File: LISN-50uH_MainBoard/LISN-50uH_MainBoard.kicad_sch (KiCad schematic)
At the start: 85 parts, among them J1 Faston Tab 4.8mm, J10 Conn_Coaxial, J11 Conn_01x03_Pin, J2 Faston Tab 4.8mm, J3 Faston Tab 4.8mm, J4 Faston Tab 4.8mm, J5 Conn_Coaxial, J6 Conn_Coaxial, J7 Faston Tab 4.8mm, J8 Faston Tab 4.8mm, J9 Conn_Coaxial, SW1 SW_DPDT_x2

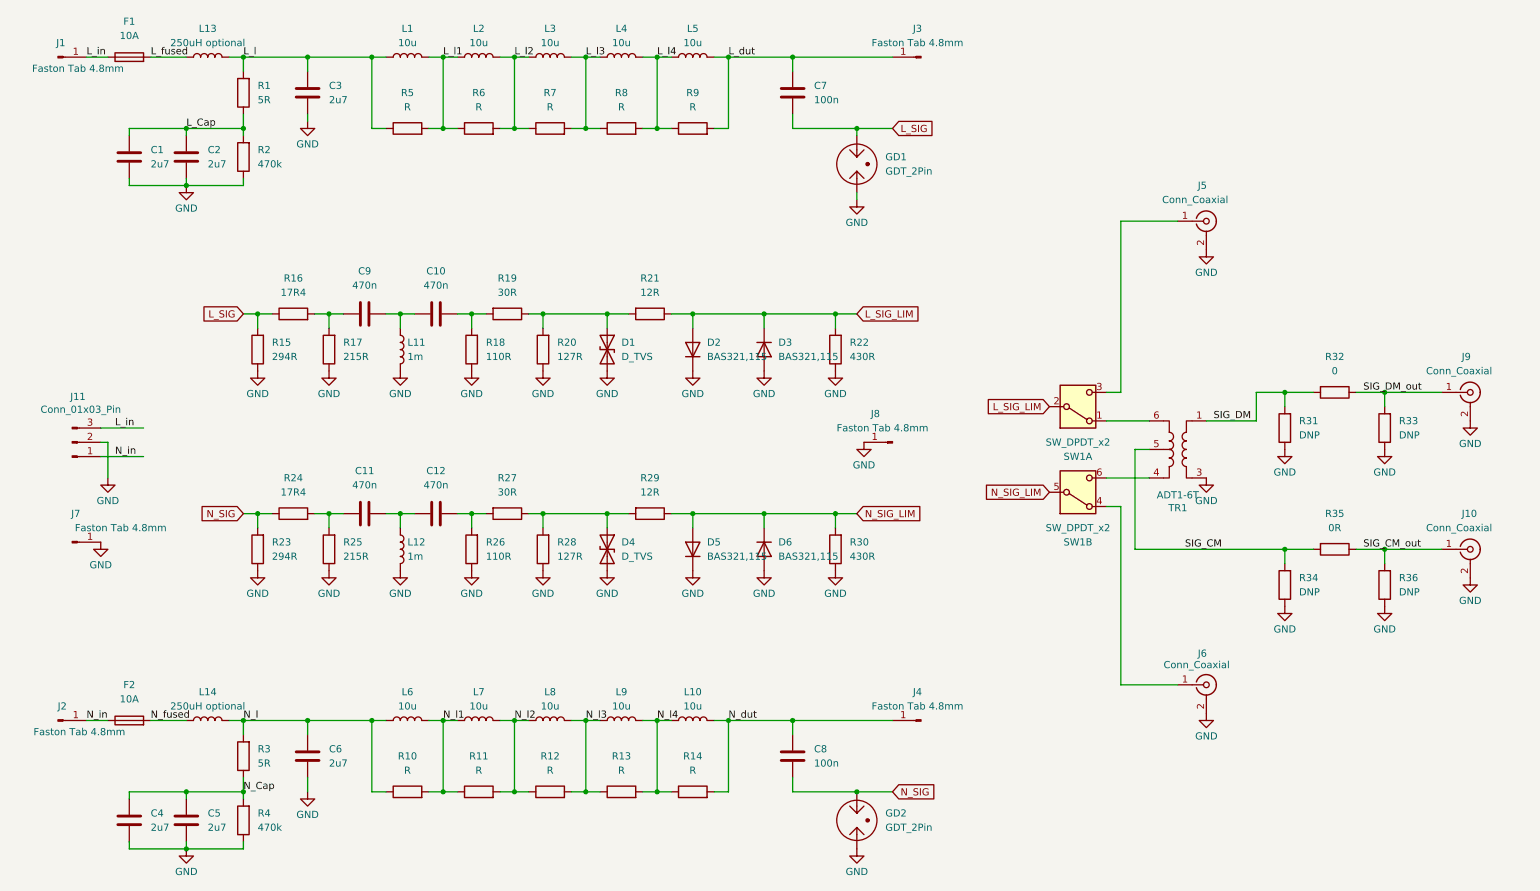
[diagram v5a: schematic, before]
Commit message: move CM DM to dedicated PCB
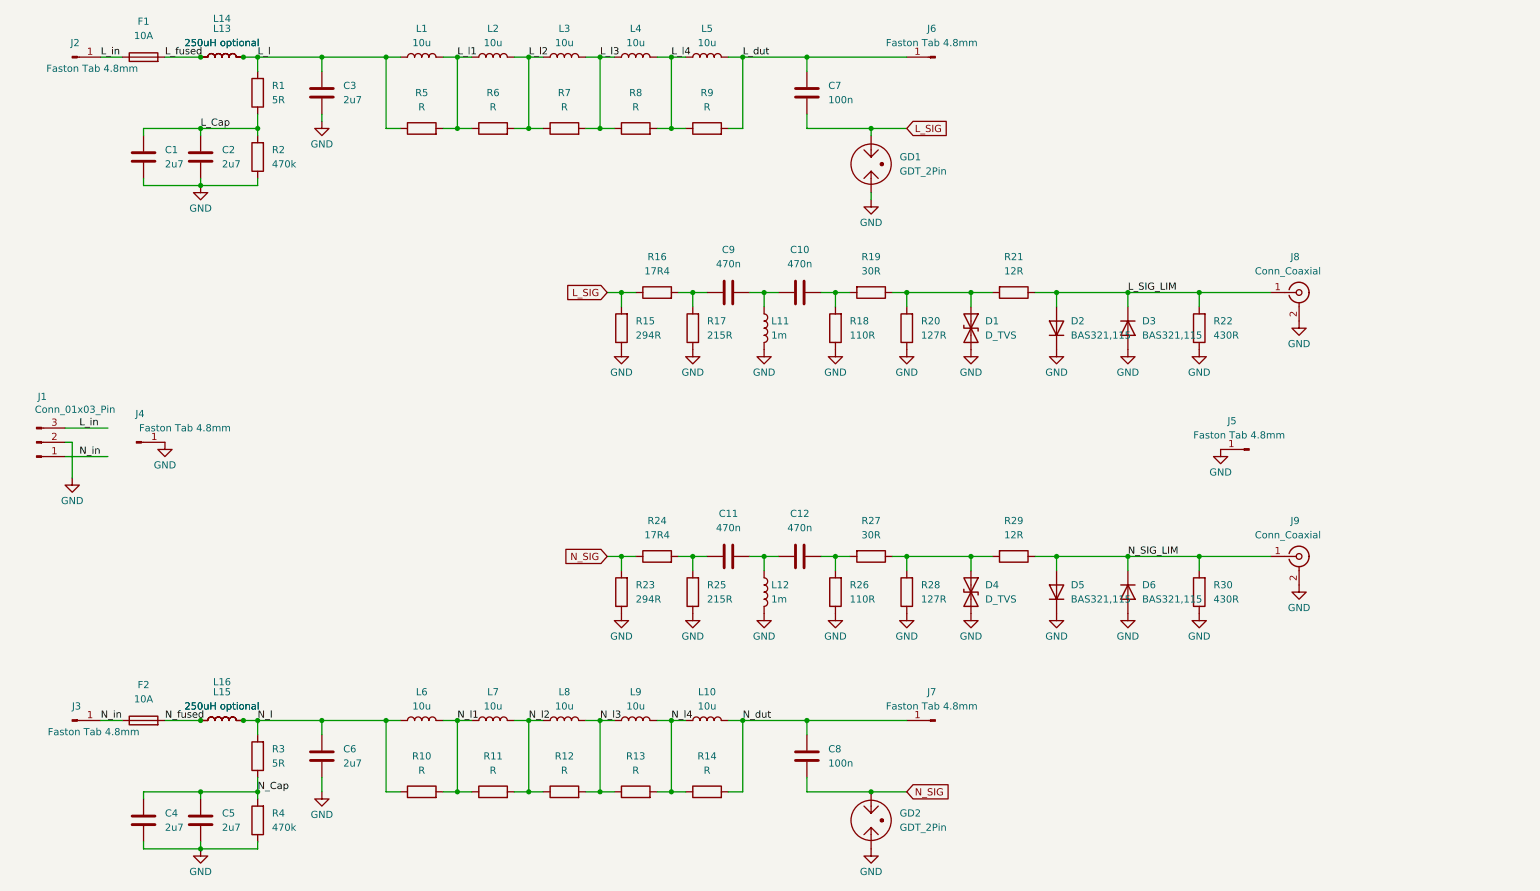
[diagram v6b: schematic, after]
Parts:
- removed J5, J6: Conn_Coaxial, Connector_Coaxial:SMA_Molex_73251-2200_Horizontal, symbol Connector:Conn_Coaxial
- removed R31, R33, R34, R36: DNP, Resistor_SMD:R_0805_2012Metric, symbol Device:R
- removed R32: 0, Resistor_SMD:R_0805_2012Metric, symbol Device:R
- removed R35: 0R, Resistor_SMD:R_0805_2012Metric, symbol Device:R
- removed SW1: SW_DPDT_x2, a_project_library:SW_E-SWITCH_LC2255EENP_DPDT_right_angle, symbol Switch:SW_DPDT_x2
- removed TR1: ADT1-6T, RF_Mini-Circuits:Mini-Circuits_CD637_H5.23mm, symbol Transformer:ADT1-6T
- added L14: 250uH optional, a_project_library:L_Toroid_Vertical_L38.0mm_W16.0mm_P15.0mm_Wuerth_WE-FI, symbol Device:L
- added L16: 250uH optional, a_project_library:L_Toroid_Horizontal_D42.0mm_H21.5mm_Abracon_ATCA-08, symbol Device:L
- L13: footprint a_project_library:L_Toroid_Vertical_L38.0mm_W16.0mm_P15.0mm_Wuerth_WE-FI -> a_project_library:L_Toroid_Horizontal_D42.0mm_H21.5mm_Abracon_ATCA-08
- renumbered J11 to J1, J1 to J2, J2 to J3, J7 to J4, J8 to J5, J3 to J6, J4 to J7, J9 to J8, J10 to J9, L14 to L15
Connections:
- net SIG_CM_out is gone; now on net N_SIG_LIM: J9.1 (In)
- net SIG_DM_out is gone; now on net L_SIG_LIM: J8.1 (In)
- net L_fused: now also L14.1
- net L_l: now also L14.2
- net N_fused: now also L16.1
- net N_l: now also L16.2
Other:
- moved on the sheet: C1, C10, C11, C12, C2, C3, C4, C5, C6, C7, C8, C9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
